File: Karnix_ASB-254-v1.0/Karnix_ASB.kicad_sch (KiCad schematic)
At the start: 58 parts, among them SW1 SW_Push, SW2 SW_Push, SW3 SW_Push, SW4 SW_Push

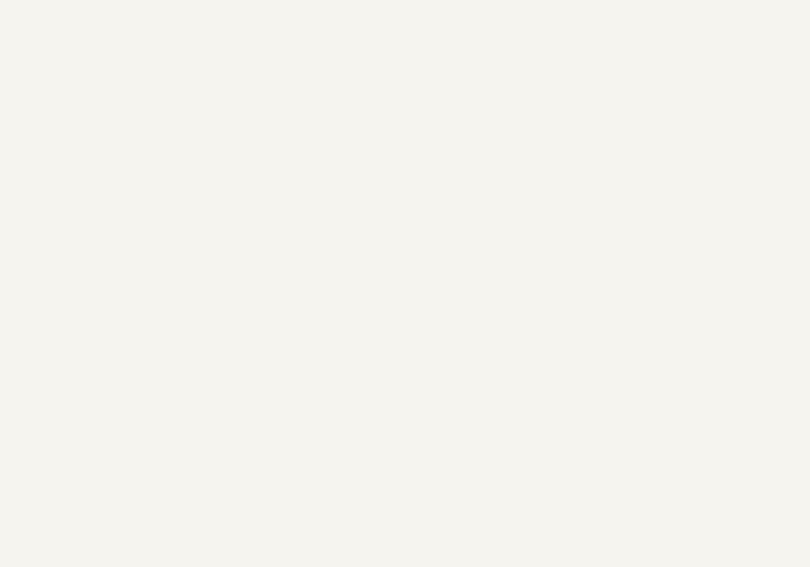
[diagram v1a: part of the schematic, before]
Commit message: Add JTAG connector making onboard programmer FT2232D optional
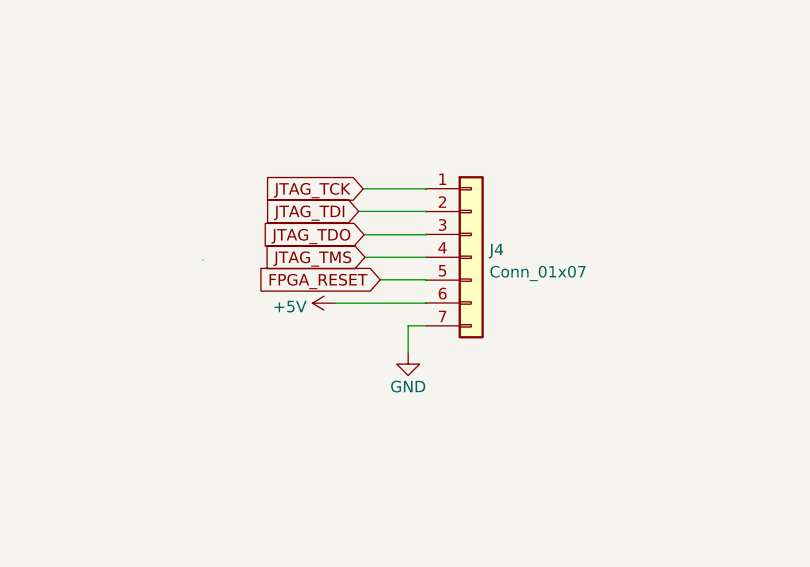
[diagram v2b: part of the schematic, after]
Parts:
- added J4: Conn_01x07, Connector_PinHeader_2.00mm:PinHeader_1x07_P2.00mm_Vertical, symbol Connector_Generic:Conn_01x07
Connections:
- net +5V: now also J4.6 (Pin_6)
- net GND: now also J4.7 (Pin_7)
- new net FPGA_RESET: J4.5 (Pin_5)
- new net JTAG_TCK: J4.1 (Pin_1)
- new net JTAG_TDI: J4.2 (Pin_2)
- new net JTAG_TDO: J4.3 (Pin_3)
- new net JTAG_TMS: J4.4 (Pin_4)
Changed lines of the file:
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@@
   (junction (at 153.035 157.607) (diameter 0) (color 0 0 0 0)
   )
+  (wire (pts (xy 244.5 184.8) (xy 244.5 181.82))
+    (stroke (width 0) (type default))
+  )
   (wire (pts (xy 266.0974 97.6461) (xy 255.9374 97.6461))
     (stroke (width 0) (type default))
@@
     (stroke (width 0) (type default))
   )
+  (wire (pts (xy 246.5 169.1) (xy 246.5 169.12))
+    (stroke (width 0) (type default))
+  )
   (wire (pts (xy 255.9374 125.6115) (xy 255.9374 125.5861))
     (stroke (width 0) (type default))
@@
     (stroke (width 0) (type default))
   )
+  (wire (pts (xy 239.7 174.2) (xy 246.42 174.2))
+    (stroke (width 0) (type default))
+  )
   (wire (pts (xy 162.687 99.949) (xy 160.147 99.949))
     (stroke (width 0) (type default))
@@
     (stroke (width 0) (type default))
   )
+  (wire (pts (xy 246.5 179.28) (xy 246.42 179.28))
+    (stroke (width 0) (type default))
+  )
   (wire (pts (xy 255.925 107.7995) (xy 255.9374 107.7995))
     (stroke (width 0) (type default))
@@
     (stroke (width 0) (type default))
   )
+  (wire (pts (xy 246.5 171.7) (xy 246.5 171.66))
+    (stroke (width 0) (type default))
+  )
   (wire (pts (xy 153.035 152.781) (xy 153.035 150.241))
     (stroke (width 0) (type default))
@@
     (stroke (width 0) (type default))
   )
+  (wire (pts (xy 239 169.1) (xy 246.5 169.1))
+    (stroke (width 0) (type default))
+  )
   (wire (pts (xy 222.9174 112.8861) (xy 212.7574 112.8861))
     (stroke (width 0) (type default))
@@
     (stroke (width 0) (type default))
   )
+  (wire (pts (xy 221.68 174.5) (xy 221.7 174.5))
+    (stroke (width 0) (type default))
+  )
   (wire (pts (xy 266.0466 130.6661) (xy 266.0466 130.6407))
     (stroke (width 0) (type default))
@@
     (stroke (width 0) (type default))
   )
+  (wire (pts (xy 236.4 179.3) (xy 246.5 179.3))
+    (stroke (width 0) (type default))
+  )
   (wire (pts (xy 153.035 167.259) (xy 153.035 164.719))
     (stroke (width 0) (type default))
   )
+  (wire (pts (xy 239.5 166.6) (xy 246.5 166.6))
+    (stroke (width 0) (type default))
+  )
   (wire (pts (xy 222.9174 120.5061) (xy 212.7574 120.5061))
     (stroke (width 0) (type default))
   )
+  (wire (pts (xy 246.5 166.6) (xy 246.5 166.58))
+    (stroke (width 0) (type default))
+  )
   (wire (pts (xy 222.9174 105.2661) (xy 212.7574 105.2661))
     (stroke (width 0) (type default))
   )
+  (wire (pts (xy 246.5 176.74) (xy 246.42 176.74))
+    (stroke (width 0) (type default))
+  )
   (wire (pts (xy 222.9174 128.1261) (xy 212.7574 128.1261))
     (stroke (width 0) (type default))
@@
     (stroke (width 0) (type default))
   )
+  (wire (pts (xy 246.5 171.66) (xy 246.42 171.66))
+    (stroke (width 0) (type default))
+  )
   (wire (pts (xy 233.0774 112.8861) (xy 243.2374 112.8861))
     (stroke (width 0) (type default))
@@
     (stroke (width 0) (type default))
   )
+  (wire (pts (xy 239.6 171.7) (xy 246.5 171.7))
+    (stroke (width 0) (type default))
+  )
   (wire (pts (xy 233.0774 97.6461) (xy 243.2374 97.6461))
     (stroke (width 0) (type default))
@@
     (stroke (width 0) (type default))
   )
+  (wire (pts (xy 246.5 169.12) (xy 246.42 169.12))
+    (stroke (width 0) (type default))
+  )
   (wire (pts (xy 154.813 164.719) (xy 153.035 164.719))
     (stroke (width 0) (type default))
   )
+  (wire (pts (xy 246.5 179.3) (xy 246.5 179.28))
+    (stroke (width 0) (type default))
+  )
   (wire (pts (xy 233.0774 92.5661) (xy 243.2374 92.5661))
     (stroke (width 0) (type default))
@@
     (stroke (width 0) (type default))
   )
+  (wire (pts (xy 246.5 176.7) (xy 246.5 176.74))
+    (stroke (width 0) (type default))
+  )
   (wire (pts (xy 130.937 150.241) (xy 130.937 142.24))
     (stroke (width 0) (type default))
@@
     (stroke (width 0) (type default))
   )
+  (wire (pts (xy 246.5 166.58) (xy 246.42 166.58))
+    (stroke (width 0) (type default))
+  )
+  (wire (pts (xy 241.4 176.7) (xy 246.5 176.7))
+    (stroke (width 0) (type default))
+  )
   (wire (pts (xy 152.527 99.949) (xy 147.447 99.949))
     (stroke (width 0) (type default))
@@
     (stroke (width 0) (type default))
   )
+  (wire (pts (xy 244.5 181.82) (xy 246.42 181.82))
+    (stroke (width 0) (type default))
+  )
   (wire (pts (xy 168.656 164.719) (xy 164.973 164.719))
     (stroke (width 0) (type default))
@@
     )
   )
+  (global_label "FPGA_RESET" (shape input) (at 241.4 176.7 180)
+    (effects (font (size 1.27 1.27)) (justify right))
+    (property "Intersheetrefs" "${INTERSHEET_REFS}" (at 241.4 176.7 0)
+      (effects (font (size 1.27 1.27)) hide)
+    )
+  )
   (global_label "GPIO_09" (shape input) (at 212.7574 112.8861 180)
     (effects (font (size 1.27 1.27)) (justify right))
@@
     )
   )
+  (global_label "JTAG_TCK" (shape input) (at 239.5 166.6 180)
+    (effects (font (size 1.27 1.27)) (justify right))
+    (property "Intersheetrefs" "${INTERSHEET_REFS}" (at 239.5 166.6 0)
+      (effects (font (size 1.27 1.27)) hide)
+    )
+  )
   (global_label "GPIO_06" (shape input) (at 212.7574 125.5861 180)
     (effects (font (size 1.27 1.27)) (justify right))
@@
     )
   )
+  (global_label "JTAG_TDI" (shape input) (at 239 169.1 180)
+    (effects (font (size 1.27 1.27)) (justify right))
+    (property "Intersheetrefs" "${INTERSHEET_REFS}" (at 239 169.1 0)
+      (effects (font (size 1.27 1.27)) hide)
+    )
+  )
   (global_label "RS485_B" (shape input) (at 85.471 124.333 0)
     (effects (font (size 1.27 1.27)) (justify left))
@@
     )
   )
+  (global_label "JTAG_TDO" (shape input) (at 239.6 171.7 180)
+    (effects (font (size 1.27 1.27)) (justify right))
+    (property "Intersheetrefs" "${INTERSHEET_REFS}" (at 239.6 171.7 0)
+      (effects (font (size 1.27 1.27)) hide)
+    )
+  )
   (global_label "OUT_AUDIO_R" (shape input) (at 184.277 230.378 0) (fields_autoplaced)
     (effects (font (size 1.27 1.27)) (justify left))
@@
     )
   )
+  (global_label "JTAG_TMS" (shape input) (at 239.7 174.2 180)
+    (effects (font (size 1.27 1.27)) (justify right))
+    (property "Intersheetrefs" "${INTERSHEET_REFS}" (at 239.7 174.2 0)
+      (effects (font (size 1.27 1.27)) hide)
+    )
+  )
   (global_label "GPIO_19" (shape input) (at 212.7574 130.6661 180)
     (effects (font (size 1.27 1.27)) (justify right))
@@
     )
   )
+  (symbol (lib_id "Connector_Generic:Conn_01x07") (at 251.5 174.2 0) (unit 1)
+    (in_bom yes) (on_board yes) (dnp no) (fields_autoplaced)
+    (property "Reference" "J4" (at 253.532 173.3881 0)
+      (effects (font (size 1.27 1.27)) (justify left))
+    )
+    (property "Value" "Conn_01x07" (at 253.532 175.8516 0)
+      (effects (font (size 1.27 1.27)) (justify left))
+    )
+    (property "Footprint" "Connector_PinHeader_2.00mm:PinHeader_1x07_P2.00mm_Vertical" (at 251.5 174.2 0)
+      (effects (font (size 1.27 1.27)) hide)
+    )
+    (property "Datasheet" "~" (at 251.5 174.2 0)
+      (effects (font (size 1.27 1.27)) hide)
+    )
+    (pin "1")
+    (pin "2")
+    (pin "3")
+    (pin "4")
+    (pin "5")
+    (pin "6")
+    (pin "7")
+    (instances
+      (project "Karnix_ASB"
+        (path "/fe37e245-9527-4c72-91fc-09b617a42f73"
+          (reference "J4") (unit 1)
+        )
+      )
+    )
+  )
   (symbol (lib_id "Fabmicro:Resistor") (at 271.1774 97.6461 180) (unit 1)
     (in_bom yes) (on_board yes) (dnp no)
@@
     )
   )
+  (symbol (lib_id "power:+5V") (at 236.4 179.3 90) (unit 1)
+    (in_bom yes) (on_board yes) (dnp no) (fields_autoplaced)
+    (property "Reference" "#PWR039" (at 240.21 179.3 0)
+      (effects (font (size 1.27 1.27)) hide)
+    )
+    (property "Value" "+5V" (at 233.2251 179.7198 90)
+      (effects (font (size 1.27 1.27)) (justify left))
+    )
+    (property "Footprint" "" (at 236.4 179.3 0)
+      (effects (font (size 1.27 1.27)) hide)
+    )
+    (property "Datasheet" "" (at 236.4 179.3 0)
+      (effects (font (size 1.27 1.27)) hide)
+    )
+    (pin "1")
+    (instances
+      (project "Karnix_ASB"
+        (path "/fe37e245-9527-4c72-91fc-09b617a42f73/00000000-0000-0000-0000-0000602e0fd3"
+          (reference "#PWR039") (unit 1)
+        )
+        (path "/fe37e245-9527-4c72-91fc-09b617a42f73"
+          (reference "#PWR0221") (unit 1)
+        )
+      )
+    )
+  )
   (symbol (lib_id "Fabmicro:Resistor") (at 227.9974 120.5061 180) (unit 1)
     (in_bom yes) (on_board yes) (dnp no)
@@
         )
       )
+    )
+  )
+  (symbol (lib_id "power:GND") (at 244.5 184.8 0) (mirror y) (unit 1)
+    (in_bom yes) (on_board yes) (dnp no)
+    (property "Reference" "#PWR?" (at 244.5 191.15 0)
+      (effects (font (size 1.27 1.27)) hide)
+    )
+    (property "Value" "GND" (at 244.5 188.61 0)
+      (effects (font (size 1.27 1.27)))
+    )
+    (property "Footprint" "" (at 244.5 184.8 0)
+      (effects (font (size 1.27 1.27)) hide)
+    )
+    (property "Datasheet" "" (at 244.5 184.8 0)
+      (effects (font (size 1.27 1.27)) hide)
+    )
+    (pin "1")
+    (instances
+      (project "Karnix_ASB"
+        (path "/fe37e245-9527-4c72-91fc-09b617a42f73/00000000-0000-0000-0000-0000602e11fa"
+          (reference "#PWR?") (unit 1)
+        )
+        (path "/fe37e245-9527-4c72-91fc-09b617a42f73/00000000-0000-0000-0000-0000602e119a"
+          (reference "#PWR063") (unit 1)
+        )
+        (path "/fe37e245-9527-4c72-91fc-09b617a42f73"
+          (reference "#PWR0137") (unit 1)
+        )
+      )
